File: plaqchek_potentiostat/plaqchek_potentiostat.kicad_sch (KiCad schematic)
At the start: 33 parts, among them J1 Conn_01x03, J2 Conn_01x03, SW1 SW_DPDT_x2, U1 Opamp_Dual, U2 L78L05_SOT89, U3 Opamp_Dual, U4 Opamp_Dual, U5 TPS7A2050PDBVR, U8 MC79M05_TO252

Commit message: finish schematic
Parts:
- removed SW1: SW_DPDT_x2, symbol Switch:SW_DPDT_x2
- removed U5: TPS7A2050PDBVR, symbol plaqchek_mlb:TPS7A2050PDBVR
- added J3: Conn_01x02, symbol Connector_Generic:Conn_01x02
- added R13, R14: 10k, symbol Device:R_Small_US
- added R15, R16, R17: 0, symbol Device:R_Small_US
- added SW2: SW_SPDT, symbol Switch:SW_SPDT
- added TP1: WE, symbol Connector:TestPoint
- added TP10: -5VA, symbol Connector:TestPoint
- added TP11: RE, symbol Connector:TestPoint
- added TP12: RDIV, symbol Connector:TestPoint
- added TP13: VBIAS_P, symbol Connector:TestPoint
- added TP2: SUM, symbol Connector:TestPoint
- added TP3: NINV_AMP, symbol Connector:TestPoint
- added TP4: TestPoint, symbol Connector:TestPoint
- added TP5: BUFF, symbol Connector:TestPoint
- added TP6: VREF, symbol Connector:TestPoint
- added TP7: BIAS_RDIV, symbol Connector:TestPoint
- added TP8: VBIAS_N, symbol Connector:TestPoint
- added TP9: 5VA, symbol Connector:TestPoint
- added U5: TPS7A2050PDBVR, symbol plaqchek:TPS7A2050PDBVR
- R1: value 1Meg -> 100kR
- R6: value R_Variable_US -> 100kR
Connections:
- net +5VA: now also R15.1; no longer C10.1
- net +6V: now also R17.2, U5.1 (IN)
- net -5VA: now also R16.1; no longer C31.2, U8.3 (VO)
- net GND: now also J3.2 (Pin_2), U5.2 (GND)
- net REF_ELEC: now also TP11.1
- net VBIAS_POT: now also SW2.2 (B), TP4.1
- net VBIAS_POT_N: now also SW2.1 (A), TP8.1
- net VBIAS_POT_P: now also SW2.3 (C), TP13.1
- net VDAC_POT_PWM_5V: now also J3.1 (Pin_1)
- net VREF_POT_5V: now also TP6.1
- net WORKING_ELEC: now also TP1.1
- net at R2.1, R4.2, U4.3 (+): now also TP7.1
- net at R12.2, U1.1, U1.5 (+): now also TP2.1
- net at R1.2, U3.6 (-), U3.7: now also R13.2, TP5.1
- net at R1.1, R3.2, U3.3 (+): now also R13.1, TP12.1
- net at R6.1, R7.1, U3.1: now also R14.2, TP3.1
- net at R5.2, R6.2, U3.2 (-): now also R14.1
- new net: R17.1, U5.3 (EN)
- new net: C31.2, R16.2, TP10.1, U8.3 (VO)
- new net: C10.1, R15.2, TP9.1, U5.5 (OUT)
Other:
- moved on the sheet: C10, C2, C3, C4, C9, J1, R1, R10, R12, R2, R3, R5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

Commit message: finish main logic board PCB routing
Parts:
- removed U1, U3, U4: Opamp_Dual, symbol Device:Opamp_Dual
- added U1, U3, U4: TL082, Package_TO_SOT_SMD:TSOT-23-8_HandSoldering, symbol Amplifier_Operational:TL082
- C1, C10, C2, C26, C3, C31, C4, C5, C6, C7, C8, C9: footprint (none) -> Capacitor_SMD:C_0603_1608Metric_Pad1.08x0.95mm_HandSolder
- J1, J2: footprint (none) -> Connector_PinHeader_2.54mm:PinHeader_1x03_P2.54mm_Vertical
- J3: footprint (none) -> Connector_PinHeader_2.54mm:PinHeader_1x02_P2.54mm_Vertical
- R1, R6: value 100kR -> 100kR_adj
- R10, R11, R12, R13, R14, R15, R16, R17, R3, R4, R5, R7, R8, R9: footprint (none) -> Resistor_SMD:R_0603_1608Metric_Pad0.98x0.95mm_HandSolder
- R2: value 1Meg -> 1Meg_adj
- U5: footprint (none) -> Package_TO_SOT_SMD:SOT-23-5_HandSoldering
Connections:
- net +5VA: now also U1.8 (V+), U3.8 (V+), U4.8 (V+)
- net -5VA: now also U1.4 (V-), U3.4 (V-), U4.4 (V-)
- net GND: now also U4.5 (+)
- net REF_ELEC: now also U3.6 (-)
- net VBIAS_POT_N: now also U4.7
- net VBIAS_POT_P: now also U4.1, U4.2 (-)
- net WORKING_ELEC: now also U3.7
- net at R2.1, R4.2, TP7.1: now also U4.3 (+)
- net at R1.2, R13.2, TP5.1: now also U1.1, U1.2 (-)
- net at R12.2, TP2.1: now also U3.1, U3.5 (+)
- net at R10.2, R12.1: now also U3.2 (-)
- net at R7.2, R8.2: now also U3.3 (+)
- net at R1.1, R13.1, R3.2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: now also U1.5 (+)
- net at R11.2, R9.1: now also U4.6 (-)
- net at R14.2, R6.1, R7.1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: now also U1.7
- net at R14.1, R5.2, R6.2: now also U1.6 (-)
- net VDAC_POT_PWM_5V renamed VDAC_POT_PWM_3V3
- net VDAC_POT_PWM_3V3: now also U1.3 (+)

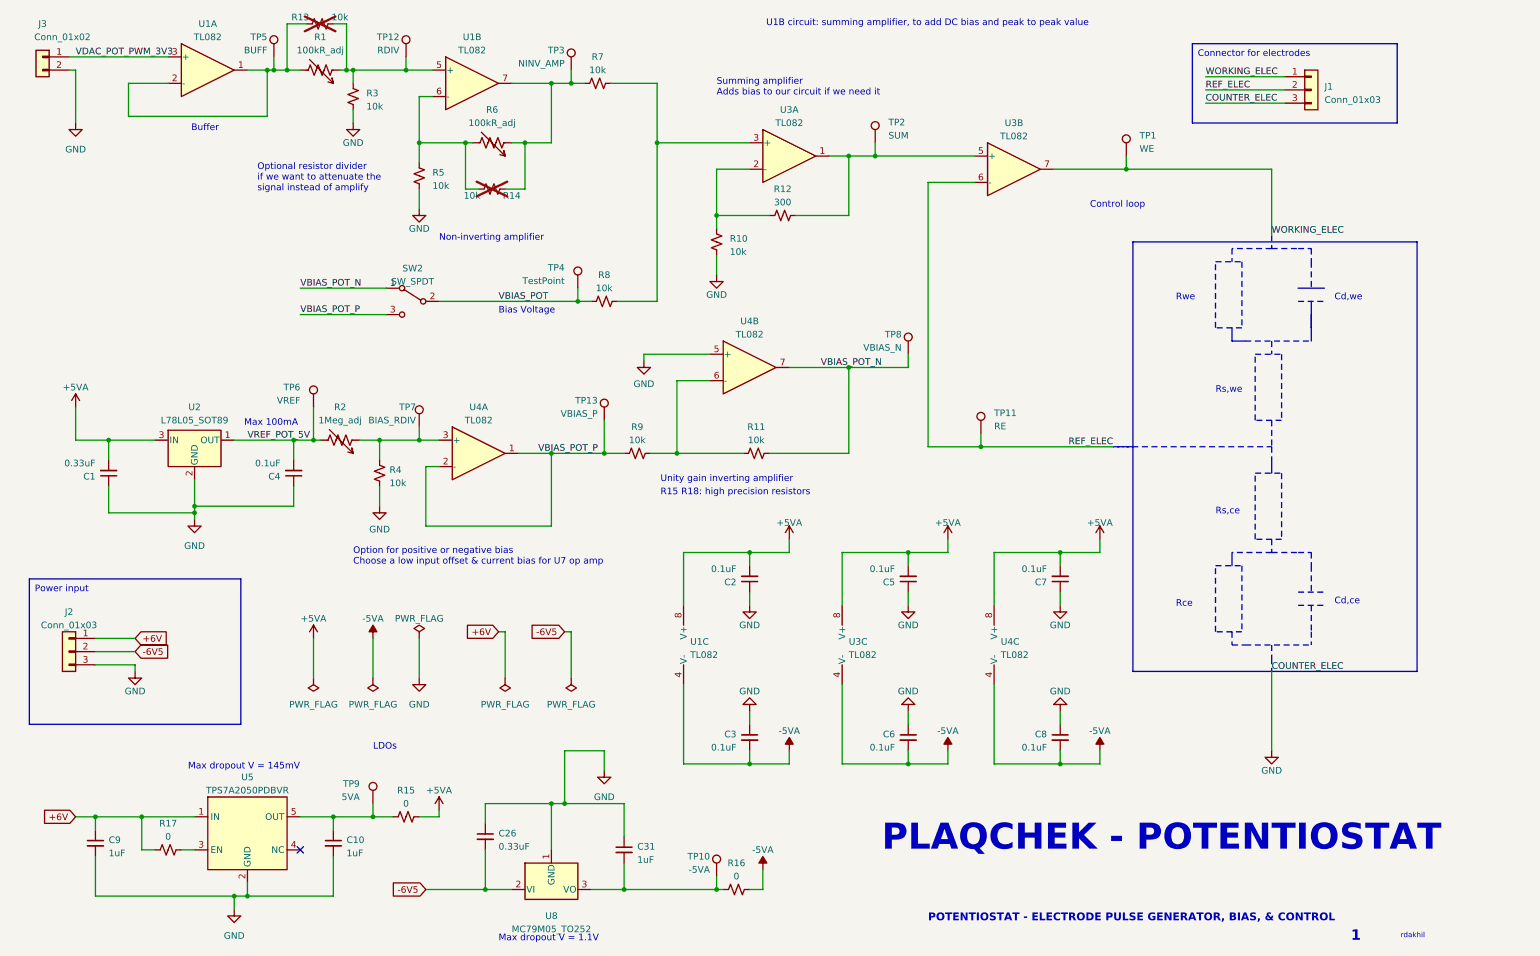
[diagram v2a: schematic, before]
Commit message: more routing for potentiostat board
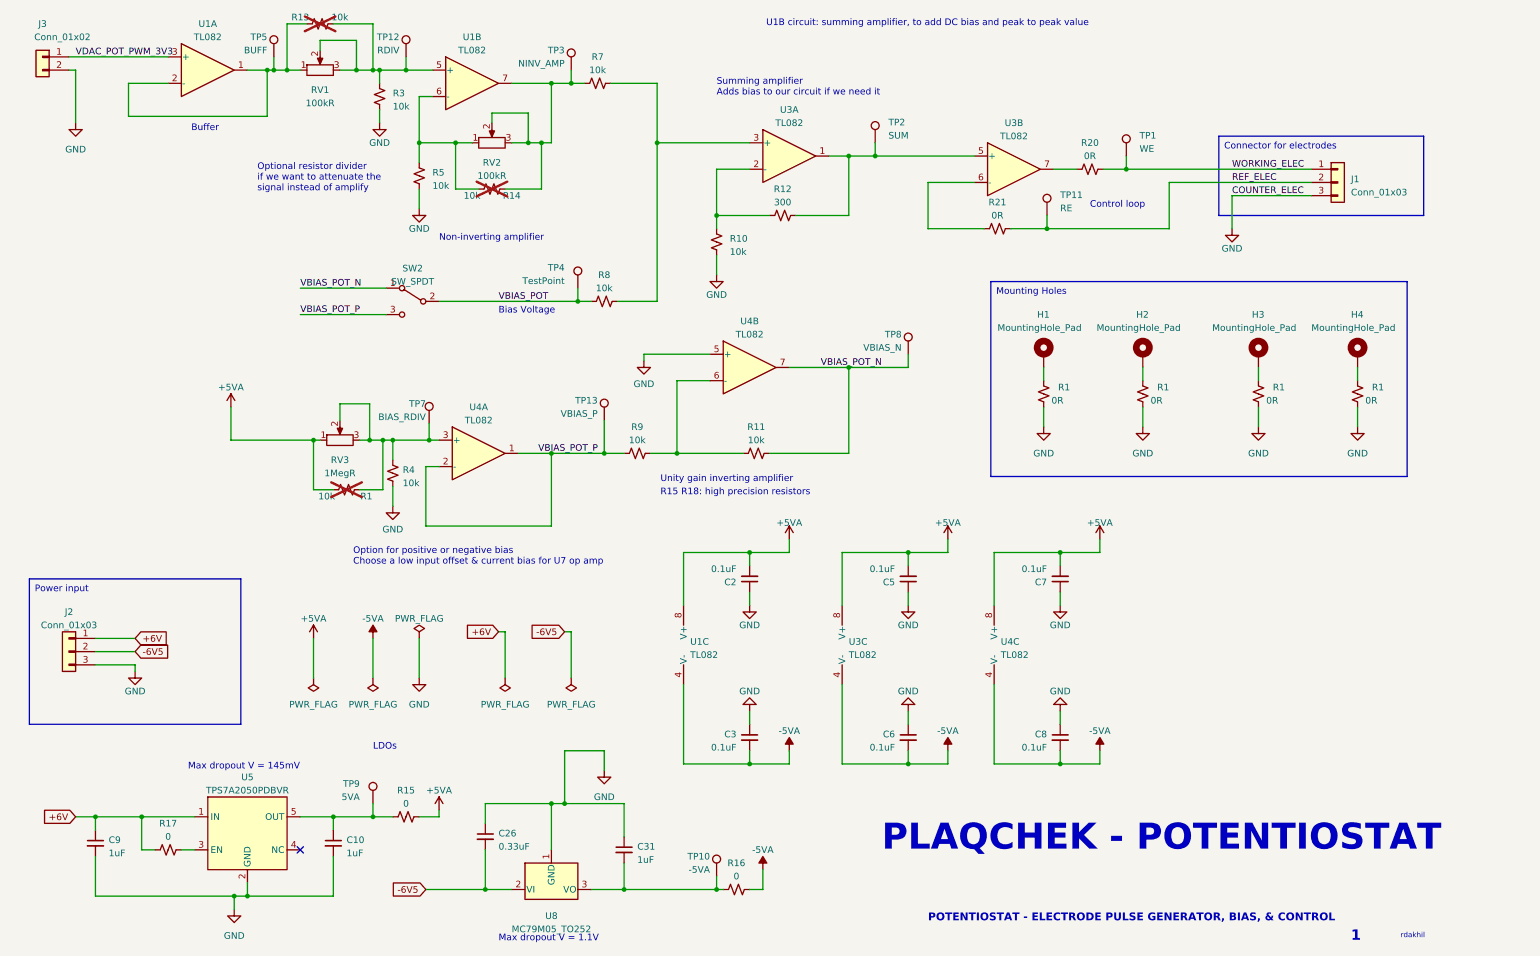
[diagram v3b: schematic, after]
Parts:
- removed C1: 0.33uF, Capacitor_SMD:C_0603_1608Metric_Pad1.08x0.95mm_HandSolder, symbol Device:C_Small
- removed C4: 0.1uF, Capacitor_SMD:C_0603_1608Metric_Pad1.08x0.95mm_HandSolder, symbol Device:C_Small
- removed R1, R6: 100kR_adj, symbol Device:R_Variable_US
- removed R2: 1Meg_adj, symbol Device:R_Variable_US
- removed TP6: VREF, symbol Connector:TestPoint
- removed U2: L78L05_SOT89, Package_TO_SOT_SMD:SOT-89-3, symbol Regulator_Linear:L78L05_SOT89
- added H1, H2, H3, H4: MountingHole_Pad, MountingHole:MountingHole_3.2mm_M3_Pad, symbol Mechanical:MountingHole_Pad
- added R1 (x4), R20, R21: 0R, Resistor_SMD:R_0603_1608Metric_Pad0.98x0.95mm_HandSolder, symbol Device:R_Small_US
- added R1: 10k, Resistor_SMD:R_0603_1608Metric_Pad0.98x0.95mm_HandSolder, symbol Device:R_Small_US
- added RV1, RV2: 100kR, Potentiometer_THT:Potentiometer_Bourns_3296Y_Vertical, symbol Device:R_Potentiometer
- added RV3: 1MegR, Potentiometer_THT:Potentiometer_Bourns_3296W_Vertical, symbol Device:R_Potentiometer
- SW2: footprint (none) -> Button_Switch_THT:SW_Slide_1P2T_CK_OS102011MS2Q
- TP1, TP10, TP11, TP12, TP13, TP2, TP3, TP4, TP5, TP7, TP8, TP9: footprint (none) -> TestPoint:TestPoint_Pad_D1.0mm
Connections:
- net +5VA: now also R1.1, RV3.1
- net GND: now also R1.2, R1.2, R1.2, R1.2
- net REF_ELEC: now also R21.1; no longer U3.6 (-)
- net WORKING_ELEC: now also R20.1; no longer U3.7
- net at R13.2, TP5.1, U1.1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: now also RV1.1
- net at R13.1, R3.2, TP12.1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: now also RV1.2, RV1.3
- net at R4.2, TP7.1, U4.3 (+): now also R1.2, RV3.2, RV3.3
- net at R14.2, R7.1, TP3.1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: now also RV2.2, RV2.3
- net at R14.1, R5.2, U1.6 (-): now also RV2.1
- new net: H4.1, R1.1
- new net: R21.2, U3.6 (-)
- new net: R20.2, U3.7
- new net: H3.1, R1.1
- new net: H2.1, R1.1
- new net: H1.1, R1.1
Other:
- note removed: "Cd,ce"
- note removed: "Cd,we"
- note removed: "Max 100mA"
- note removed: "Rce"
- note removed: "Rs,ce"
- note removed: "Rs,we"
- note removed: "Rwe"
- moved on the sheet: J1, R3, R4, TP11, TP7

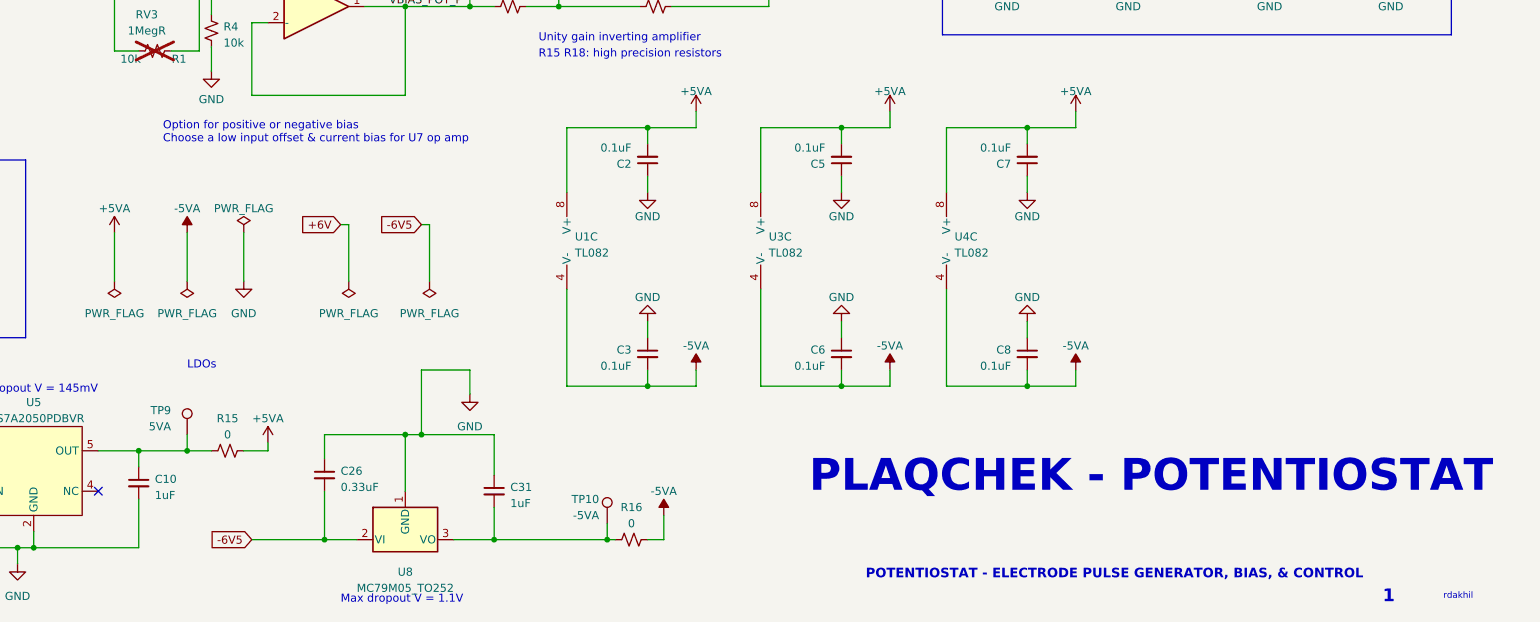
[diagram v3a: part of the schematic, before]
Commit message: finish potentiostat board, update board constraints
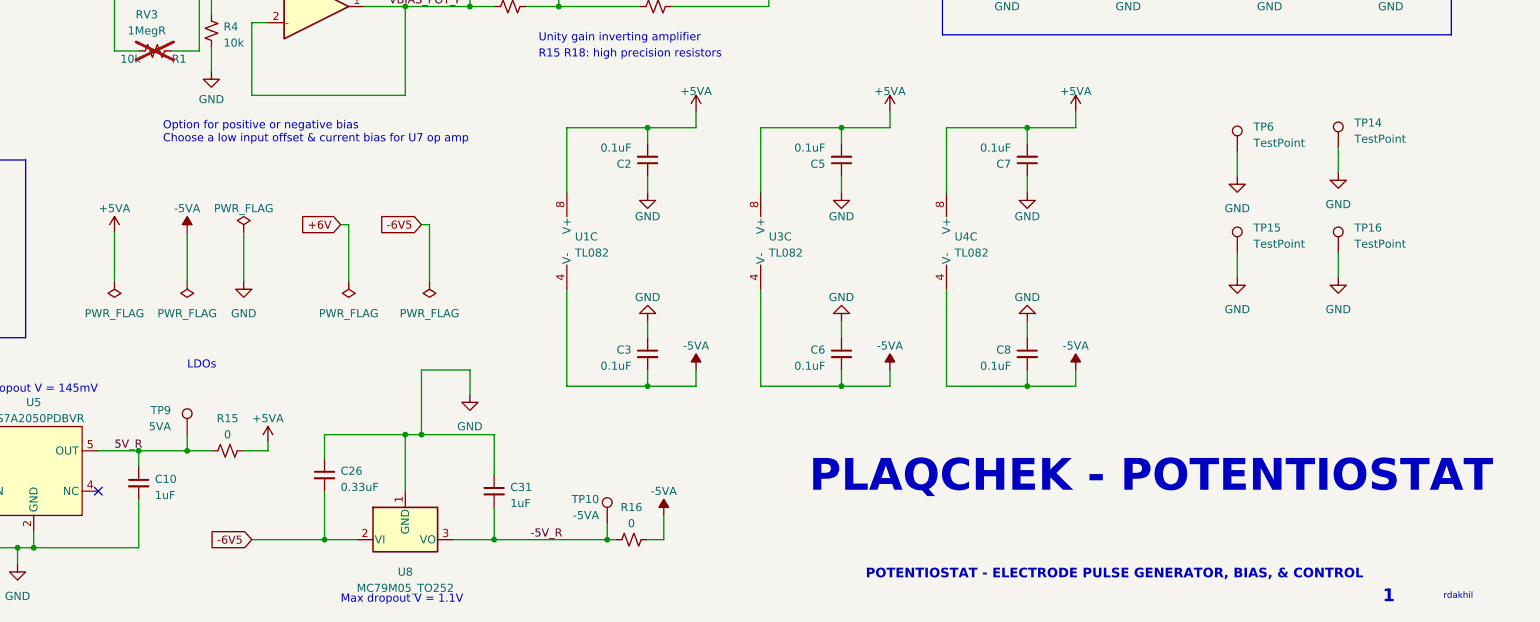
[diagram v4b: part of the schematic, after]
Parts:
- added TP14, TP15, TP16, TP6: TestPoint, TestPoint:TestPoint_Pad_D1.0mm, symbol Connector:TestPoint
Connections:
- net GND: now also TP14.1, TP15.1, TP16.1, TP6.1
- net -5V_R: now reaches C31.2, R16.2, TP10.1, U8.3 (VO)
- net 5V_R: now reaches C10.1, R15.2, TP9.1, U5.5 (OUT)
